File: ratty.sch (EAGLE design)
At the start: 89 parts, among them IC2 L293DD, Q1 BS170, Q2 BS170, Q3 BS170, Q5 BS170, U1 ITG-32001:1

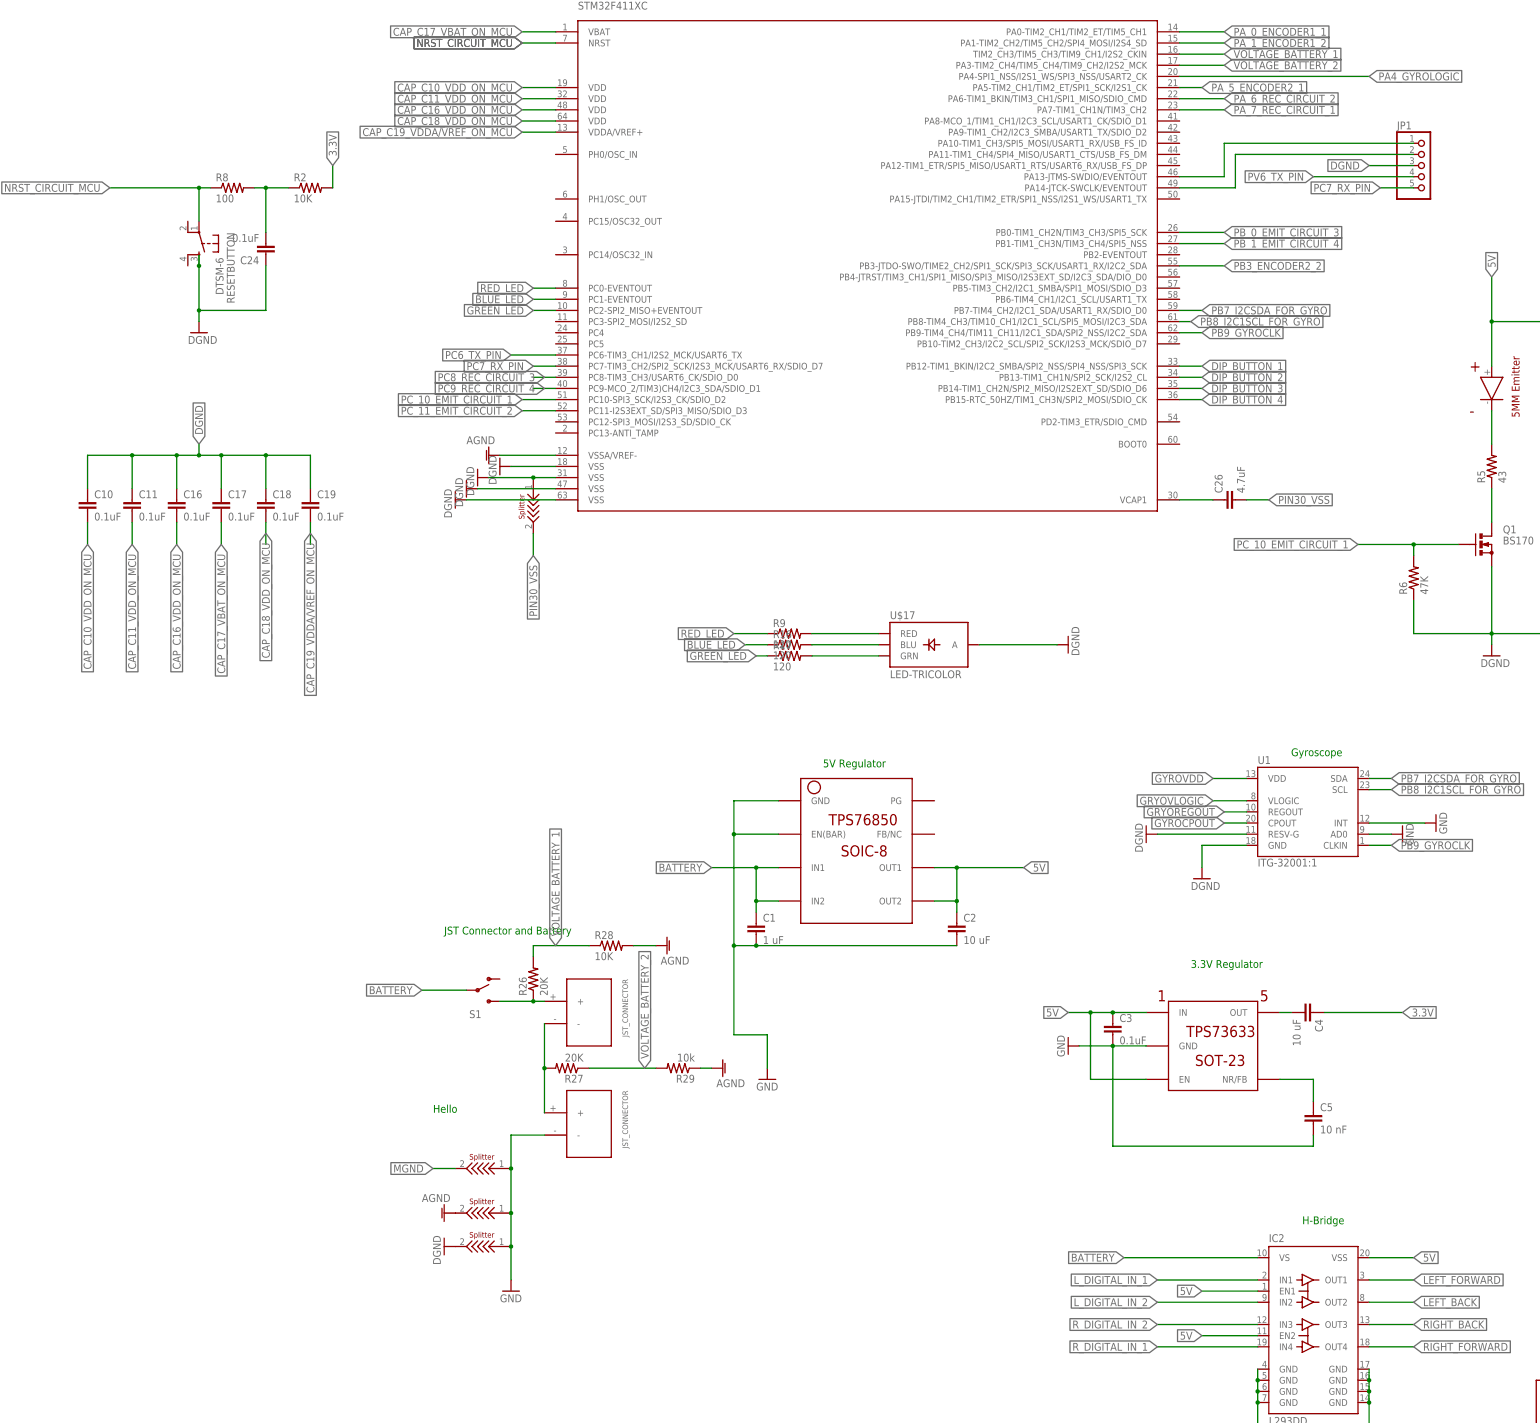
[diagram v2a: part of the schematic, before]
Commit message: Fixed hbridge whoops
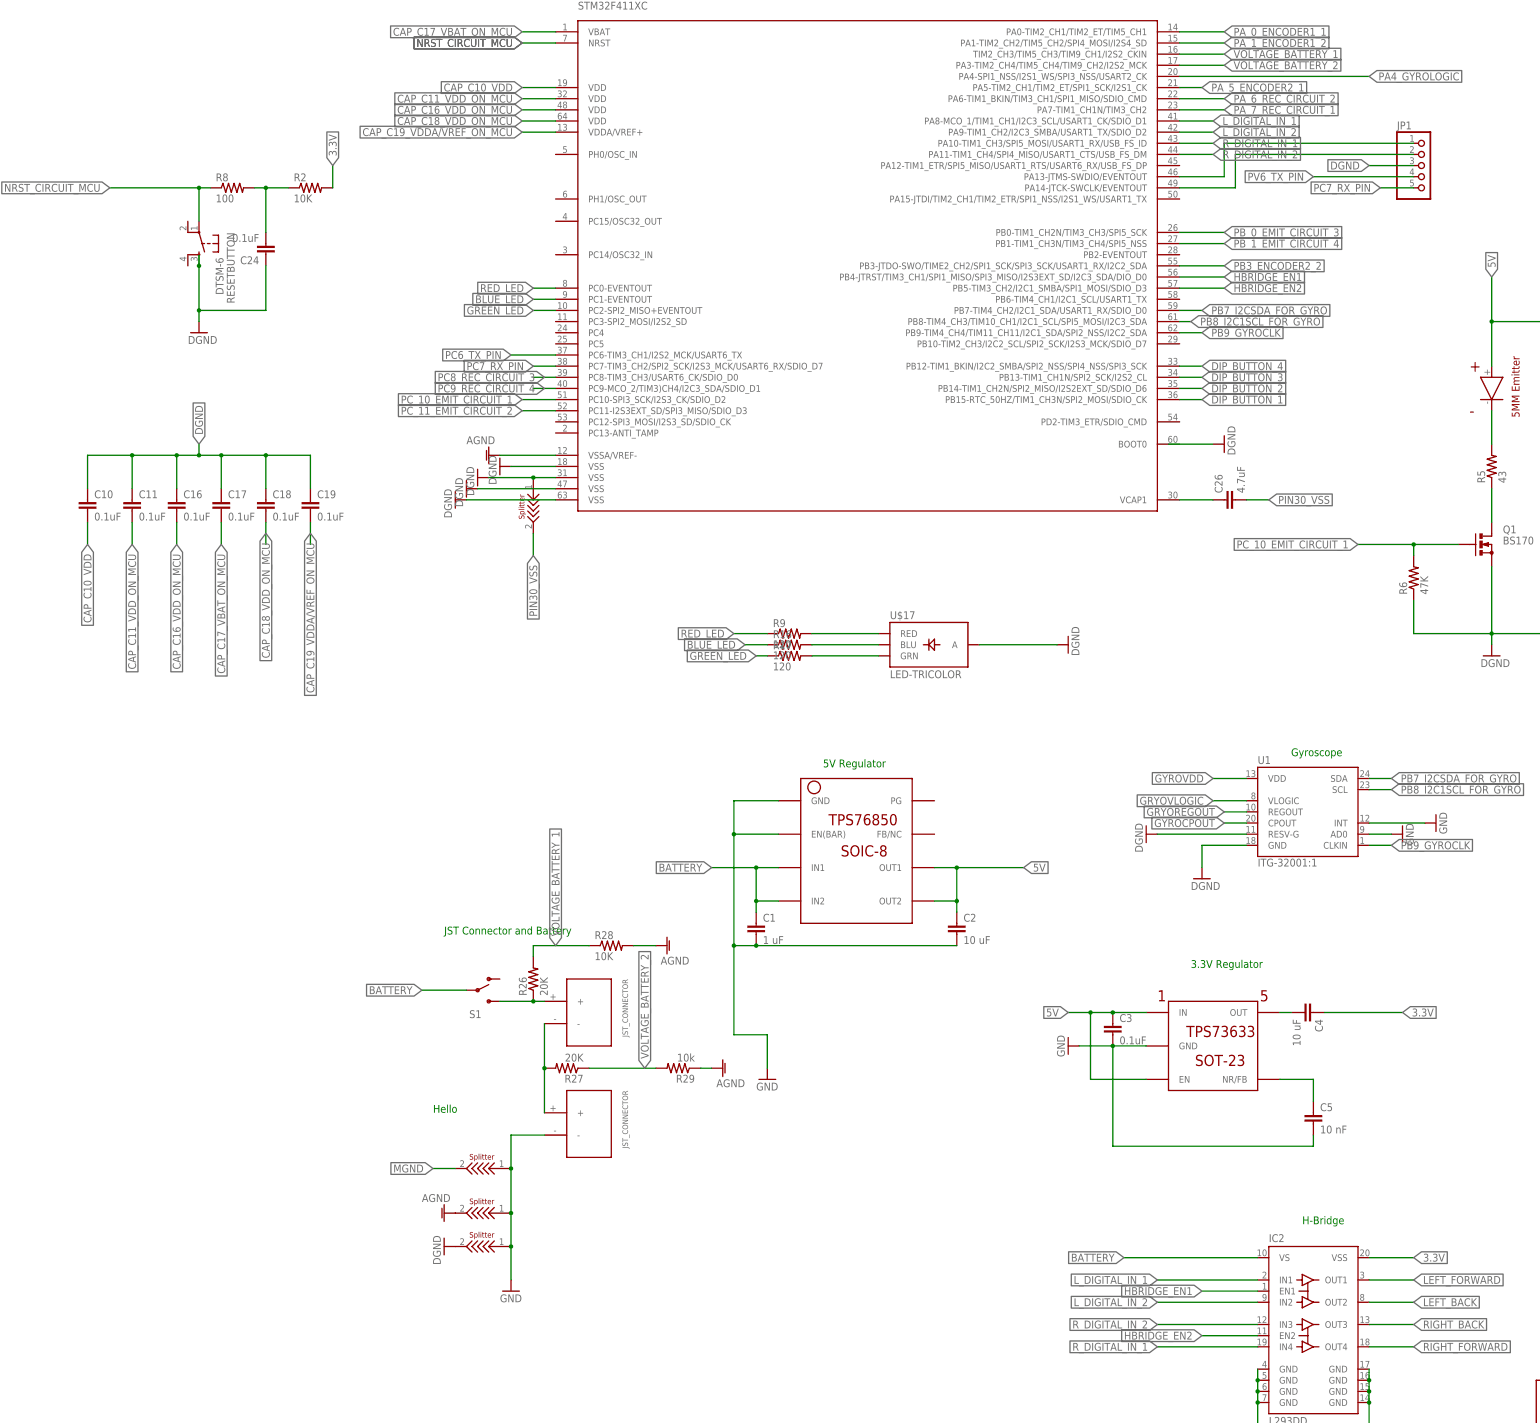
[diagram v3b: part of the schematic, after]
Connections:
- net CAP_C10_VDD_ON_MCU renamed CAP_C10_VDD
- new net HBRIDGE_EN1: IC2.EN1, U$4.PB4-JTRST/TIM3_CH1/SPI1_MISO/SPI3_MISO/I2S3EXT_SD/I2C3_SDA/DIO_D0
- new net HBRIDGE_EN2: IC2.EN2, U$4.PB5-TIM3_CH2/I2C1_SMBA/SPI1_MOSI/SDIO_D3
- net 3.3V: now also IC2.VSS
- net 5V: no longer IC2.EN1, IC2.EN2, IC2.VSS
- net DIP_BUTTON_1: now also U$4.PB15-RTC_50HZ/TIM1_CH3N/SPI2_MOSI/SDIO_CK; no longer U$4.PB12-TIM1_BKIN/I2C2_SMBA/SPI2_NSS/SPI4_NSS/SPI3_SCK
- net DIP_BUTTON_2: now also U$4.PB14-TIM1_CH2N/SPI2_MISO/I2S2EXT_SD/SDIO_D6; no longer U$4.PB13-TIM1_CH1N/SPI2_SCK/I2S2_CL
- net DIP_BUTTON_3: now also U$4.PB13-TIM1_CH1N/SPI2_SCK/I2S2_CL; no longer U$4.PB14-TIM1_CH2N/SPI2_MISO/I2S2EXT_SD/SDIO_D6
- net DIP_BUTTON_4: now also U$4.PB12-TIM1_BKIN/I2C2_SMBA/SPI2_NSS/SPI4_NSS/SPI3_SCK; no longer U$4.PB15-RTC_50HZ/TIM1_CH3N/SPI2_MOSI/SDIO_CK
- net L_DIGITAL_IN_1: now also U$4.PA8-MCO_1/TIM1_CH1/I2C3_SCL/USART1_CK/SDIO_D1
- net L_DIGITAL_IN_2: now also U$4.PA9-TIM1_CH2/I2C3_SMBA/USART1_TX/SDIO_D2
- net R_DIGITAL_IN_1: now also U$4.PA10-TIM1_CH3/SPI5_MOSI/USART1_RX/USB_FS_ID
- net R_DIGITAL_IN_2: now also U$4.PA11-TIM1_CH4/SPI4_MISO/USART1_CTS/USB_FS_DM
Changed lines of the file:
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@@
 <?xml version="1.0" encoding="utf-8"?>
 <!DOCTYPE eagle SYSTEM "eagle.dtd">
-<eagle version="7.7.0">
+<eagle version="7.5.0">
 <drawing>
 <settings>
@@
 <part name="R29" library="rcl" deviceset="R-US_" device="R0603" value="10k"/>
 <part name="AGND8" library="supply1" deviceset="AGND" device=""/>
+<part name="GND27" library="SparkFun-Aesthetics" deviceset="DGND" device=""/>
 </parts>
 <sheets>
@@
 <instance part="R29" gate="G$1" x="88.9" y="93.98" rot="R180"/>
 <instance part="AGND8" gate="VR1" x="99.06" y="93.98" rot="R90"/>
+<instance part="GND27" gate="G$1" x="213.36" y="236.22" rot="R90"/>
 </instances>
 <busses>
@@
 </segment>
 <segment>
-<pinref part="IC2" gate="G$1" pin="EN1"/>
-<wire x1="220.98" y1="43.18" x2="208.28" y2="43.18" width="0.1524" layer="91"/>
-<label x="208.28" y="43.18" size="1.778" layer="95" rot="MR0" xref="yes"/>
-</segment>
-<segment>
-<pinref part="IC2" gate="G$1" pin="EN2"/>
-<wire x1="220.98" y1="33.02" x2="208.28" y2="33.02" width="0.1524" layer="91"/>
-<label x="208.28" y="33.02" size="1.778" layer="95" rot="MR0" xref="yes"/>
-</segment>
-<segment>
-<pinref part="IC2" gate="G$1" pin="VSS"/>
-<wire x1="246.38" y1="50.8" x2="256.54" y2="50.8" width="0.1524" layer="91"/>
-<label x="256.54" y="50.8" size="1.778" layer="95" xref="yes"/>
-</segment>
-<segment>
 <pinref part="SPLIT_GYRO_VDD" gate="G$1" pin="2"/>
 <wire x1="350.52" y1="172.72" x2="350.52" y2="175.26" width="0.1524" layer="91"/>
@@
 <label x="198.12" y="40.64" size="1.778" layer="95" rot="MR0" xref="yes"/>
 </segment>
+<segment>
+<pinref part="U$4" gate="G$1" pin="PA9-TIM1_CH2/I2C3_SMBA/USART1_TX/SDIO_D2"/>
+<wire x1="203.2" y1="307.34" x2="210.82" y2="307.34" width="0.1524" layer="91"/>
+<label x="210.82" y="307.34" size="1.778" layer="95" xref="yes"/>
+</segment>
 </net>
 <net name="L_DIGITAL_IN_1" class="0">
@@
 <label x="198.12" y="45.72" size="1.778" layer="95" rot="MR0" xref="yes"/>
 </segment>
+<segment>
+<pinref part="U$4" gate="G$1" pin="PA8-MCO_1/TIM1_CH1/I2C3_SCL/USART1_CK/SDIO_D1"/>
+<wire x1="203.2" y1="309.88" x2="210.82" y2="309.88" width="0.1524" layer="91"/>
+<label x="210.82" y="309.88" size="1.778" layer="95" xref="yes"/>
+</segment>
 </net>
 <net name="R_DIGITAL_IN_1" class="0">
@@
 <label x="198.12" y="30.48" size="1.778" layer="95" rot="MR0" xref="yes"/>
 </segment>
+<segment>
+<pinref part="U$4" gate="G$1" pin="PA10-TIM1_CH3/SPI5_MOSI/USART1_RX/USB_FS_ID"/>
+<wire x1="203.2" y1="304.8" x2="210.82" y2="304.8" width="0.1524" layer="91"/>
+<label x="210.82" y="304.8" size="1.778" layer="95" xref="yes"/>
+</segment>
 </net>
 <net name="R_DIGITAL_IN_2" class="0">
@@
 <wire x1="220.98" y1="35.56" x2="198.12" y2="35.56" width="0.1524" layer="91"/>
 <label x="198.12" y="35.56" size="1.778" layer="95" rot="MR0" xref="yes"/>
+</segment>
+<segment>
+<pinref part="U$4" gate="G$1" pin="PA11-TIM1_CH4/SPI4_MISO/USART1_CTS/USB_FS_DM"/>
+<wire x1="203.2" y1="302.26" x2="210.82" y2="302.26" width="0.1524" layer="91"/>
+<label x="210.82" y="302.26" size="1.778" layer="95" xref="yes"/>
 </segment>
 </net>
@@
 <wire x1="502.92" y1="322.58" x2="502.92" y2="347.98" width="0.1524" layer="91"/>
 <label x="502.92" y="347.98" size="1.778" layer="95" rot="R90" xref="yes"/>
+</segment>
+<segment>
+<pinref part="IC2" gate="G$1" pin="VSS"/>
+<wire x1="246.38" y1="50.8" x2="256.54" y2="50.8" width="0.1524" layer="91"/>
+<label x="256.54" y="50.8" size="1.778" layer="95" xref="yes"/>
 </segment>
 </net>
@@
 </segment>
 </net>
-<net name="CAP_C10_VDD_ON_MCU" class="0">
+<net name="CAP_C10_VDD" class="0">
 <segment>
 <wire x1="60.96" y1="317.5" x2="53.34" y2="317.5" width="0.1524" layer="91"/>
@@
 <junction x="408.94" y="302.26"/>
 <pinref part="GND26" gate="G$1" pin="GND"/>
+</segment>
+<segment>
+<wire x1="200.66" y1="236.22" x2="210.82" y2="236.22" width="0.1524" layer="91"/>
+<pinref part="GND27" gate="G$1" pin="GND"/>
 </segment>
 </net>
@@
 <net name="DIP_BUTTON_1" class="0">
 <segment>
-<pinref part="U$4" gate="G$1" pin="PB12-TIM1_BKIN/I2C2_SMBA/SPI2_NSS/SPI4_NSS/SPI3_SCK"/>
-<wire x1="203.2" y1="254" x2="208.28" y2="254" width="0.1524" layer="91"/>
-<label x="208.28" y="254" size="1.778" layer="95" xref="yes"/>
-</segment>
-<segment>
 <pinref part="S2" gate="G$1" pin="1"/>
 <wire x1="408.94" y1="320.04" x2="408.94" y2="322.58" width="0.1524" layer="91"/>
@@
 <label x="388.62" y="322.58" size="1.778" layer="95" rot="R180" xref="yes"/>
 </segment>
+<segment>
+<pinref part="U$4" gate="G$1" pin="PB15-RTC_50HZ/TIM1_CH3N/SPI2_MOSI/SDIO_CK"/>
+<wire x1="203.2" y1="246.38" x2="208.28" y2="246.38" width="0.1524" layer="91"/>
+<label x="208.28" y="246.38" size="1.778" layer="95" xref="yes"/>
+</segment>
 </net>
 <net name="DIP_BUTTON_2" class="0">
-<segment>
-<pinref part="U$4" gate="G$1" pin="PB13-TIM1_CH1N/SPI2_SCK/I2S2_CL"/>
-<wire x1="203.2" y1="251.46" x2="208.28" y2="251.46" width="0.1524" layer="91"/>
-<label x="208.28" y="251.46" size="1.778" layer="95" xref="yes"/>
-</segment>
 <segment>
 <pinref part="S2" gate="G$1" pin="2"/>
@@
 <label x="388.62" y="325.12" size="1.778" layer="95" rot="R180" xref="yes"/>
 </segment>
-</net>
-<net name="DIP_BUTTON_3" class="0">
 <segment>
 <pinref part="U$4" gate="G$1" pin="PB14-TIM1_CH2N/SPI2_MISO/I2S2EXT_SD/SDIO_D6"/>
@@
 <label x="208.28" y="248.92" size="1.778" layer="95" xref="yes"/>
 </segment>
+</net>
+<net name="DIP_BUTTON_3" class="0">
 <segment>
 <pinref part="S2" gate="G$1" pin="3"/>
@@
 <label x="388.62" y="327.66" size="1.778" layer="95" rot="R180" xref="yes"/>
 </segment>
+<segment>
+<pinref part="U$4" gate="G$1" pin="PB13-TIM1_CH1N/SPI2_SCK/I2S2_CL"/>
+<wire x1="203.2" y1="251.46" x2="208.28" y2="251.46" width="0.1524" layer="91"/>
+<label x="208.28" y="251.46" size="1.778" layer="95" xref="yes"/>
+</segment>
 </net>
 <net name="DIP_BUTTON_4" class="0">
-<segment>
-<pinref part="U$4" gate="G$1" pin="PB15-RTC_50HZ/TIM1_CH3N/SPI2_MOSI/SDIO_CK"/>
-<wire x1="203.2" y1="246.38" x2="208.28" y2="246.38" width="0.1524" layer="91"/>
-<label x="208.28" y="246.38" size="1.778" layer="95" xref="yes"/>
-</segment>
 <segment>
 <pinref part="S2" gate="G$1" pin="4"/>
@@
 <label x="388.62" y="335.28" size="1.778" layer="95" rot="R180" xref="yes"/>
 </segment>
+<segment>
+<pinref part="U$4" gate="G$1" pin="PB12-TIM1_BKIN/I2C2_SMBA/SPI2_NSS/SPI4_NSS/SPI3_SCK"/>
+<wire x1="203.2" y1="254" x2="208.28" y2="254" width="0.1524" layer="91"/>
+<label x="208.28" y="254" size="1.778" layer="95" xref="yes"/>
+</segment>
 </net>
 <net name="VOLTAGE_BATTERY_1" class="0">
@@
 </segment>
 </net>
+<net name="HBRIDGE_EN1" class="0">
+<segment>
+<pinref part="U$4" gate="G$1" pin="PB4-JTRST/TIM3_CH1/SPI1_MISO/SPI3_MISO/I2S3EXT_SD/I2C3_SDA/DIO_D0"/>
+<wire x1="203.2" y1="274.32" x2="213.36" y2="274.32" width="0.1524" layer="91"/>
+<label x="213.36" y="274.32" size="1.778" layer="95" xref="yes"/>
+</segment>
+<segment>
+<pinref part="IC2" gate="G$1" pin="EN1"/>
+<wire x1="220.98" y1="43.18" x2="208.28" y2="43.18" width="0.1524" layer="91"/>
+<label x="208.28" y="43.18" size="1.778" layer="95" rot="MR0" xref="yes"/>
+</segment>
+</net>
+<net name="HBRIDGE_EN2" class="0">
+<segment>
+<pinref part="U$4" gate="G$1" pin="PB5-TIM3_CH2/I2C1_SMBA/SPI1_MOSI/SDIO_D3"/>
+<wire x1="203.2" y1="271.78" x2="213.36" y2="271.78" width="0.1524" layer="91"/>
+<label x="213.36" y="271.78" size="1.778" layer="95" xref="yes"/>
+</segment>
+<segment>
+<pinref part="IC2" gate="G$1" pin="EN2"/>
+<wire x1="220.98" y1="33.02" x2="208.28" y2="33.02" width="0.1524" layer="91"/>
+<label x="208.28" y="33.02" size="1.778" layer="95" rot="MR0" xref="yes"/>
+</segment>
+</net>

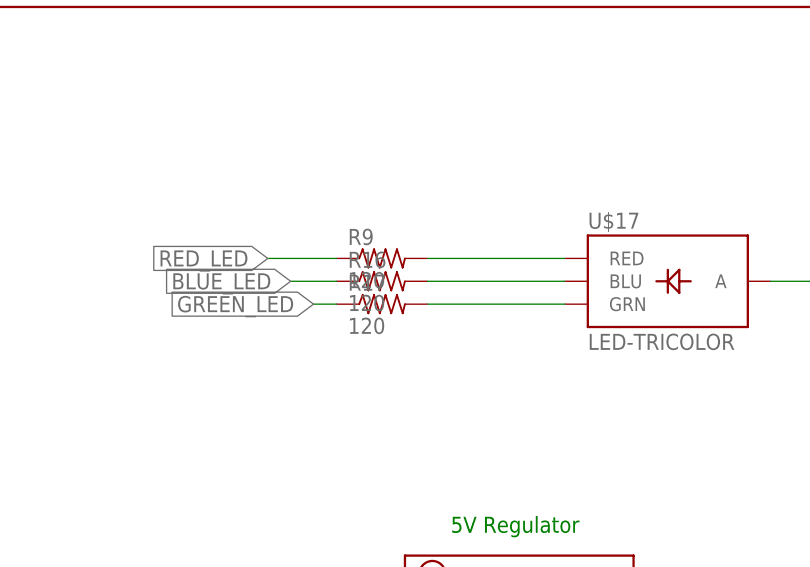
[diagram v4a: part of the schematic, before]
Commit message: Routing started, renamed some unnamed parts.
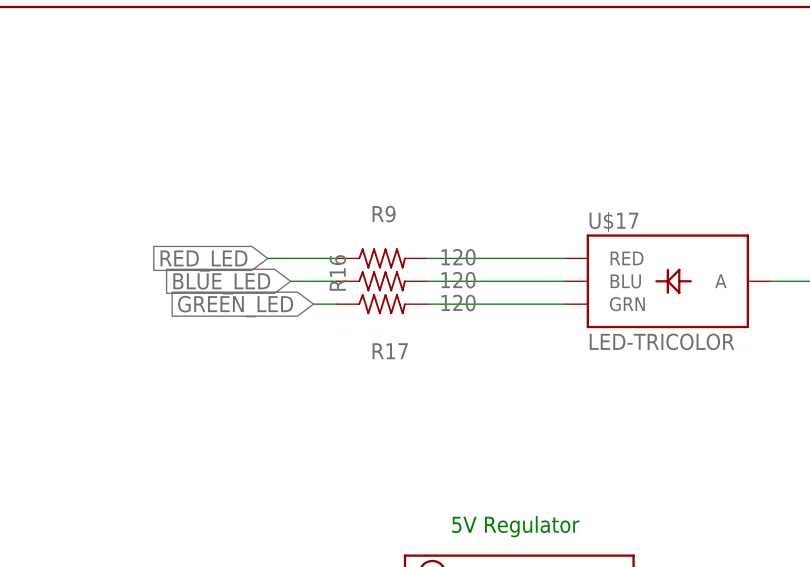
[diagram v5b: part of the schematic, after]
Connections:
- net N$1 renamed BATTERY_2
- net N$10 renamed TO_Q2_MOS
- net N$12 renamed TO_Q3_MOS
- net N$15 renamed TO_Q5_MOS
- net N$17 renamed TO_R18/C25
- net N$22 renamed TO_R20/C27
- net N$29 renamed TO_R19/C28
- net N$3 renamed TO_C5_CAP
- net N$30 renamed TO_R22/C29
- net N$4 renamed BATTERY_1
- net N$5 renamed TO_C4_CAP
- net N$7 renamed TO_Q1_MOS
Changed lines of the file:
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@@
 <instance part="U$17" gate="G$1" x="144.78" y="193.04"/>
 <instance part="GND15" gate="G$1" x="177.8" y="190.5" rot="R90"/>
-<instance part="R9" gate="G$1" x="114.3" y="193.04"/>
-<instance part="R16" gate="G$1" x="114.3" y="190.5"/>
-<instance part="R17" gate="G$1" x="114.3" y="187.96"/>
+<instance part="R9" gate="G$1" x="114.3" y="193.04" smashed="yes">
+<attribute name="NAME" x="113.03" y="197.0786" size="1.778" layer="95"/>
+<attribute name="VALUE" x="120.65" y="192.278" size="1.778" layer="96"/>
+</instance>
+<instance part="R16" gate="G$1" x="114.3" y="190.5" smashed="yes">
+<attribute name="NAME" x="110.2614" y="189.23" size="1.778" layer="95" rot="R90"/>
+<attribute name="VALUE" x="120.65" y="189.738" size="1.778" layer="96"/>
+</instance>
+<instance part="R17" gate="G$1" x="114.3" y="187.96" smashed="yes">
+<attribute name="NAME" x="113.03" y="181.8386" size="1.778" layer="95"/>
+<attribute name="VALUE" x="120.65" y="187.198" size="1.778" layer="96"/>
+</instance>
 <instance part="S2" gate="G$1" x="406.4" y="312.42" rot="R180"/>
 <instance part="R20" gate="G$1" x="408.94" y="335.28"/>
@@
 </busses>
 <nets>
-<net name="N$1" class="0">
+<net name="BATTERY_2" class="0">
 <segment>
 <pinref part="U$1" gate="G$1" pin="-"/>
@@
 </segment>
 </net>
-<net name="N$4" class="0">
+<net name="BATTERY_1" class="0">
 <segment>
 <pinref part="U$1" gate="G$1" pin="+"/>
@@
 </segment>
 </net>
-<net name="N$5" class="0">
+<net name="TO_C4_CAP" class="0">
 <segment>
 <pinref part="U$5" gate="G$1" pin="OUT"/>
@@
 </segment>
 </net>
-<net name="N$3" class="0">
+<net name="TO_C5_CAP" class="0">
 <segment>
 <pinref part="U$5" gate="G$1" pin="NR/FB"/>
@@
 </segment>
 </net>
-<net name="N$7" class="0">
+<net name="TO_Q1_MOS" class="0">
 <segment>
 <pinref part="R5" gate="G$1" pin="1"/>
@@
 </segment>
 </net>
-<net name="N$10" class="0">
+<net name="TO_Q2_MOS" class="0">
 <segment>
 <pinref part="R7" gate="G$1" pin="1"/>
@@
 </segment>
 </net>
-<net name="N$12" class="0">
+<net name="TO_Q3_MOS" class="0">
 <segment>
 <pinref part="R11" gate="G$1" pin="1"/>
@@
 </segment>
 </net>
-<net name="N$15" class="0">
+<net name="TO_Q5_MOS" class="0">
 <segment>
 <pinref part="R14" gate="G$1" pin="1"/>
@@
 </segment>
 </net>
-<net name="N$22" class="0">
+<net name="TO_R20/C27" class="0">
 <segment>
 <pinref part="R20" gate="G$1" pin="2"/>
@@
 </segment>
 </net>
-<net name="N$17" class="0">
+<net name="TO_R18/C25" class="0">
 <segment>
 <pinref part="R18" gate="G$1" pin="2"/>
@@
 </segment>
 </net>
-<net name="N$29" class="0">
+<net name="TO_R19/C28" class="0">
 <segment>
 <pinref part="R19" gate="G$1" pin="2"/>
@@
 </segment>
 </net>
-<net name="N$30" class="0">
+<net name="TO_R22/C29" class="0">
 <segment>
 <pinref part="R22" gate="G$1" pin="2"/>
